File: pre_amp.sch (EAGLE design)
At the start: 51 parts, among them Q1 BF245, Q2 BF245, Q3 BF245

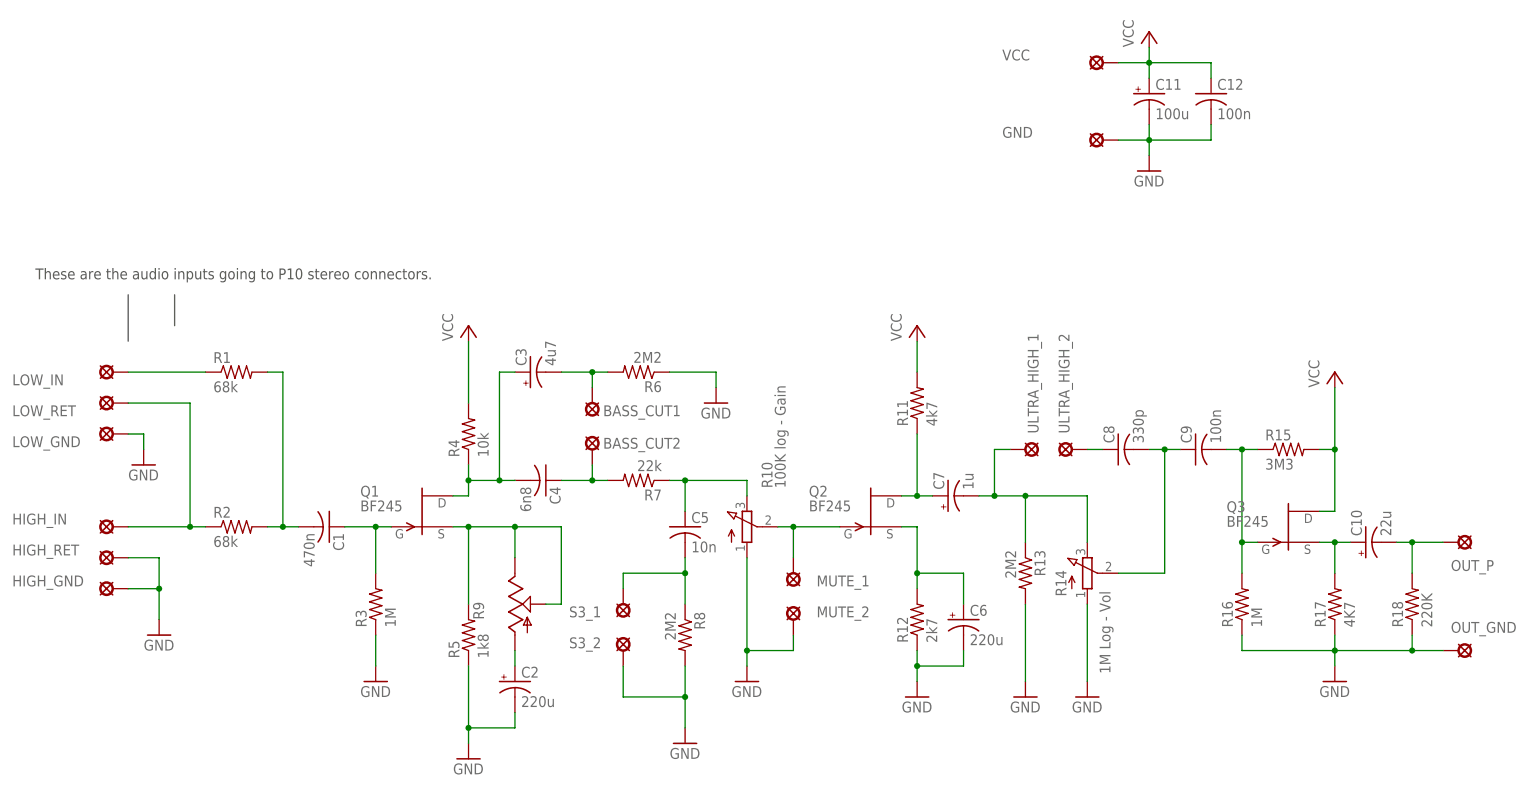
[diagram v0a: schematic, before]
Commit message: [#1] Improvements and fixes
Fixes ERC check errors:
R9 value set;
Approved FRAME have no value.

Better positioning some labels and texts.
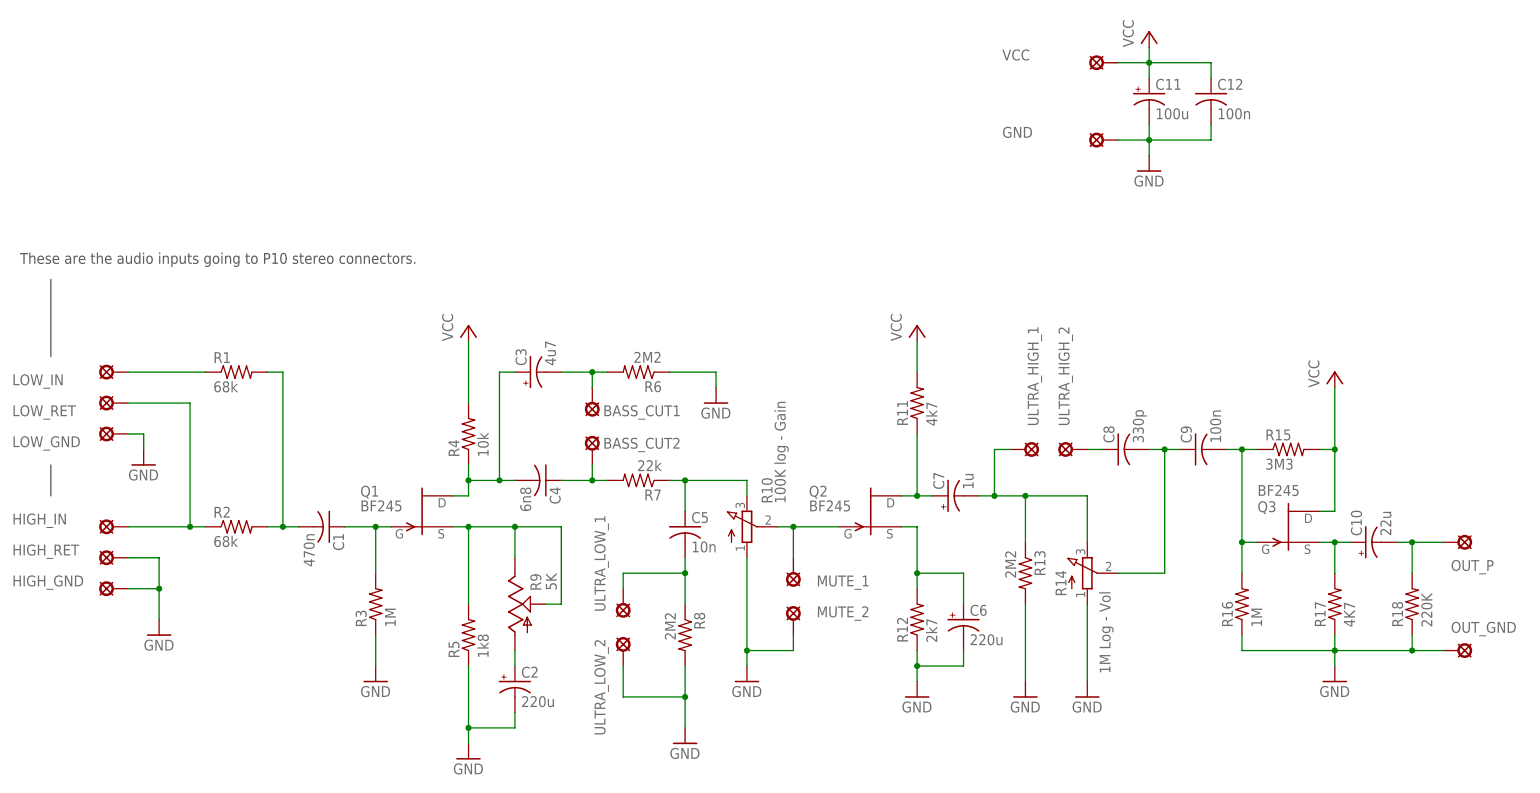
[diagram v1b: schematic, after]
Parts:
- R9: value (none) -> 5K
- renumbered S3_1 to ULTRA_LOW_1, S3_2 to ULTRA_LOW_2
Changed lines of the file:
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@@
 <part name="GND6" library="supply1" deviceset="GND" device=""/>
 <part name="P+1" library="supply1" deviceset="VCC" device=""/>
-<part name="R9" library="pot" deviceset="TRIM_US-" device="CA6V"/>
+<part name="R9" library="pot" deviceset="TRIM_US-" device="CA6V" value="5K"/>
 <part name="R10" library="pot" deviceset="3RP/1610N" device="" value="100K log - Gain"/>
 <part name="BASS_CUT1" library="solpad" deviceset="MCS08" device=""/>
 <part name="BASS_CUT2" library="solpad" deviceset="MCS08" device=""/>
-<part name="S3_1" library="solpad" deviceset="MCS08" device=""/>
-<part name="S3_2" library="solpad" deviceset="MCS08" device=""/>
+<part name="ULTRA_LOW_1" library="solpad" deviceset="MCS08" device=""/>
+<part name="ULTRA_LOW_2" library="solpad" deviceset="MCS08" device=""/>
 <part name="MUTE_1" library="solpad" deviceset="MCS08" device=""/>
 <part name="MUTE_2" library="solpad" deviceset="MCS08" device=""/>
@@
 <sheet>
 <plain>
-<text x="10.16" y="111.76" size="1.778" layer="97">These are the audio inputs going to P10 stereo connectors.</text>
-<wire x1="33.02" y1="109.22" x2="33.02" y2="104.14" width="0.1524" layer="97"/>
-<wire x1="25.4" y1="101.6" x2="25.4" y2="109.22" width="0.1524" layer="97"/>
+<text x="7.62" y="114.3" size="1.778" layer="97">These are the audio inputs going to P10 stereo connectors.</text>
+<wire x1="12.7" y1="81.28" x2="12.7" y2="76.2" width="0.1524" layer="97"/>
+<wire x1="12.7" y1="99.06" x2="12.7" y2="111.76" width="0.1524" layer="97"/>
 </plain>
 <instances>
@@
 <instance part="Q1" gate="G$1" x="73.66" y="73.66"/>
 <instance part="Q2" gate="G$1" x="147.32" y="73.66"/>
-<instance part="Q3" gate="G$1" x="215.9" y="71.12"/>
+<instance part="Q3" gate="G$1" x="215.9" y="71.12" smashed="yes">
+<attribute name="NAME" x="210.82" y="73.533" size="1.778" layer="95"/>
+<attribute name="VALUE" x="210.82" y="76.2" size="1.778" layer="96"/>
+</instance>
 <instance part="C4" gate="G$1" x="93.98" y="78.74" rot="R270"/>
 <instance part="C5" gate="G$1" x="116.84" y="71.12"/>
@@
 <instance part="GND6" gate="1" x="121.92" y="91.44"/>
 <instance part="P+1" gate="VCC" x="81.28" y="104.14"/>
-<instance part="R9" gate="G$1" x="88.9" y="58.42"/>
+<instance part="R9" gate="G$1" x="88.9" y="58.42" smashed="yes">
+<attribute name="NAME" x="91.44" y="63.5" size="1.778" layer="95" rot="R270"/>
+<attribute name="VALUE" x="93.98" y="63.5" size="1.778" layer="96" rot="R270"/>
+</instance>
 <instance part="R10" gate="G$1" x="127" y="71.12" smashed="yes">
-<attribute name="NAME" x="131.191" y="77.47" size="1.778" layer="95" rot="R90"/>
-<attribute name="VALUE" x="133.35" y="77.47" size="1.778" layer="96" rot="R90"/>
+<attribute name="NAME" x="131.191" y="74.93" size="1.778" layer="95" rot="R90"/>
+<attribute name="VALUE" x="133.35" y="74.93" size="1.778" layer="96" rot="R90"/>
 </instance>
 <instance part="BASS_CUT1" gate="G$1" x="101.6" y="91.44" smashed="yes" rot="R180">
@@
 <attribute name="NAME" x="103.378" y="83.947" size="1.778" layer="95"/>
 </instance>
-<instance part="S3_1" gate="G$1" x="106.68" y="58.42" smashed="yes" rot="R180">
-<attribute name="NAME" x="97.79" y="56.261" size="1.778" layer="95"/>
-</instance>
-<instance part="S3_2" gate="G$1" x="106.68" y="50.8" smashed="yes">
-<attribute name="NAME" x="97.79" y="51.181" size="1.778" layer="95"/>
+<instance part="ULTRA_LOW_1" gate="G$1" x="106.68" y="58.42" smashed="yes" rot="R180">
+<attribute name="NAME" x="103.759" y="57.15" size="1.778" layer="95" rot="R90"/>
+</instance>
+<instance part="ULTRA_LOW_2" gate="G$1" x="106.68" y="50.8" smashed="yes">
+<attribute name="NAME" x="103.759" y="36.83" size="1.778" layer="95" rot="R90"/>
 </instance>
 <instance part="MUTE_1" gate="G$1" x="134.62" y="63.5" smashed="yes" rot="R180">
@@
 <instance part="GND10" gate="1" x="182.88" y="43.18"/>
 <instance part="ULTRA_HIGH_2" gate="G$1" x="180.34" y="83.82" smashed="yes" rot="R90">
-<attribute name="NAME" x="178.181" y="102.87" size="1.778" layer="95" rot="R270"/>
+<attribute name="NAME" x="179.959" y="87.63" size="1.778" layer="95" rot="R90"/>
 </instance>
 <instance part="ULTRA_HIGH_1" gate="G$1" x="172.72" y="83.82" smashed="yes" rot="R270">
-<attribute name="NAME" x="173.101" y="102.87" size="1.778" layer="95" rot="R270"/>
+<attribute name="NAME" x="174.879" y="87.63" size="1.778" layer="95" rot="R90"/>
 </instance>
 <instance part="C9" gate="G$1" x="200.66" y="83.82" rot="R90"/>
@@
 <pinref part="GND5" gate="1" pin="GND"/>
 <wire x1="116.84" y1="48.26" x2="116.84" y2="43.18" width="0.1524" layer="91"/>
-<pinref part="S3_2" gate="G$1" pin="MP"/>
+<pinref part="ULTRA_LOW_2" gate="G$1" pin="MP"/>
 <wire x1="116.84" y1="43.18" x2="116.84" y2="38.1" width="0.1524" layer="91"/>
 <wire x1="106.68" y1="48.26" x2="106.68" y2="43.18" width="0.1524" layer="91"/>
@@
 <pinref part="R8" gate="G$1" pin="1"/>
 <wire x1="116.84" y1="66.04" x2="116.84" y2="63.5" width="0.1524" layer="91"/>
-<pinref part="S3_1" gate="G$1" pin="MP"/>
+<pinref part="ULTRA_LOW_1" gate="G$1" pin="MP"/>
 <wire x1="116.84" y1="63.5" x2="116.84" y2="58.42" width="0.1524" layer="91"/>
 <wire x1="106.68" y1="60.96" x2="106.68" y2="63.5" width="0.1524" layer="91"/>
@@
 </sheet>
 </sheets>
+<errors>
+</errors>
 </schematic>
 </drawing>

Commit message: [#1] Update component package
Update component package.
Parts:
- C4: device rcl:C-US375-203X418 -> rcl:C-US050-030X075
- C8: device rcl:C-US375-203X418 -> rcl:C-US050-025X075
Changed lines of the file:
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@@
 <grid distance="0.1" unitdist="inch" unit="inch" style="dots" multiple="1" display="yes" altdistance="0.01" altunitdist="inch" altunit="inch"/>
 <layers>
-<layer number="1" name="Top" color="4" fill="1" visible="no" active="no"/>
-<layer number="16" name="Bottom" color="1" fill="1" visible="no" active="no"/>
-<layer number="17" name="Pads" color="2" fill="1" visible="no" active="no"/>
-<layer number="18" name="Vias" color="2" fill="1" visible="no" active="no"/>
-<layer number="19" name="Unrouted" color="6" fill="1" visible="no" active="no"/>
-<layer number="20" name="Dimension" color="15" fill="1" visible="no" active="no"/>
-<layer number="21" name="tPlace" color="7" fill="1" visible="no" active="no"/>
-<layer number="22" name="bPlace" color="7" fill="1" visible="no" active="no"/>
-<layer number="23" name="tOrigins" color="15" fill="1" visible="no" active="no"/>
-<layer number="24" name="bOrigins" color="15" fill="1" visible="no" active="no"/>
-<layer number="25" name="tNames" color="7" fill="1" visible="no" active="no"/>
-<layer number="26" name="bNames" color="7" fill="1" visible="no" active="no"/>
-<layer number="27" name="tValues" color="7" fill="1" visible="no" active="no"/>
-<layer number="28" name="bValues" color="7" fill="1" visible="no" active="no"/>
+<layer number="1" name="Top" color="4" fill="1" visible="yes" active="no"/>
+<layer number="16" name="Bottom" color="1" fill="1" visible="yes" active="no"/>
+<layer number="17" name="Pads" color="2" fill="1" visible="yes" active="no"/>
+<layer number="18" name="Vias" color="2" fill="1" visible="yes" active="no"/>
+<layer number="19" name="Unrouted" color="6" fill="1" visible="yes" active="no"/>
+<layer number="20" name="Dimension" color="15" fill="1" visible="yes" active="no"/>
+<layer number="21" name="tPlace" color="7" fill="1" visible="yes" active="no"/>
+<layer number="22" name="bPlace" color="7" fill="1" visible="yes" active="no"/>
+<layer number="23" name="tOrigins" color="15" fill="1" visible="yes" active="no"/>
+<layer number="24" name="bOrigins" color="15" fill="1" visible="yes" active="no"/>
+<layer number="25" name="tNames" color="7" fill="1" visible="yes" active="no"/>
+<layer number="26" name="bNames" color="7" fill="1" visible="yes" active="no"/>
+<layer number="27" name="tValues" color="7" fill="1" visible="yes" active="no"/>
+<layer number="28" name="bValues" color="7" fill="1" visible="yes" active="no"/>
 <layer number="29" name="tStop" color="7" fill="3" visible="no" active="no"/>
 <layer number="30" name="bStop" color="7" fill="6" visible="no" active="no"/>
@@
 <layer number="35" name="tGlue" color="7" fill="4" visible="no" active="no"/>
 <layer number="36" name="bGlue" color="7" fill="5" visible="no" active="no"/>
-<layer number="37" name="tTest" color="7" fill="1" visible="no" active="no"/>
-<layer number="38" name="bTest" color="7" fill="1" visible="no" active="no"/>
+<layer number="37" name="tTest" color="7" fill="1" visible="yes" active="no"/>
+<layer number="38" name="bTest" color="7" fill="1" visible="yes" active="no"/>
 <layer number="39" name="tKeepout" color="4" fill="11" visible="no" active="no"/>
 <layer number="40" name="bKeepout" color="1" fill="11" visible="no" active="no"/>
@@
 <layer number="44" name="Drills" color="7" fill="1" visible="no" active="no"/>
 <layer number="45" name="Holes" color="7" fill="1" visible="no" active="no"/>
-<layer number="46" name="Milling" color="3" fill="1" visible="no" active="no"/>
-<layer number="47" name="Measures" color="7" fill="1" visible="no" active="no"/>
-<layer number="48" name="Document" color="7" fill="1" visible="no" active="no"/>
-<layer number="49" name="Reference" color="7" fill="1" visible="no" active="no"/>
-<layer number="51" name="tDocu" color="7" fill="1" visible="no" active="no"/>
-<layer number="52" name="bDocu" color="7" fill="1" visible="no" active="no"/>
+<layer number="46" name="Milling" color="3" fill="1" visible="yes" active="no"/>
+<layer number="47" name="Measures" color="7" fill="1" visible="yes" active="no"/>
+<layer number="48" name="Document" color="7" fill="1" visible="yes" active="no"/>
+<layer number="49" name="Reference" color="7" fill="1" visible="yes" active="no"/>
+<layer number="51" name="tDocu" color="7" fill="1" visible="yes" active="no"/>
+<layer number="52" name="bDocu" color="7" fill="1" visible="yes" active="no"/>
 <layer number="90" name="Modules" color="5" fill="1" visible="yes" active="yes"/>
 <layer number="91" name="Nets" color="2" fill="1" visible="yes" active="yes"/>
@@
 <part name="Q2" library="transistor-fet" deviceset="BF245" device=""/>
 <part name="Q3" library="transistor-fet" deviceset="BF245" device=""/>
-<part name="C4" library="rcl" deviceset="C-US" device="375-203X418" value="6n8"/>
+<part name="C4" library="rcl" deviceset="C-US" device="050-030X075" value="6n8"/>
 <part name="C5" library="rcl" deviceset="C-US" device="050-030X075" value="10n"/>
 <part name="LOW_IN" library="solpad" deviceset="MCS08" device=""/>
@@
 <part name="GND9" library="supply1" deviceset="GND" device=""/>
 <part name="R14" library="pot" deviceset="3RP/1610N" device="" value="1M Log - Vol"/>
-<part name="C8" library="rcl" deviceset="C-US" device="375-203X418" value="330p"/>
+<part name="C8" library="rcl" deviceset="C-US" device="050-025X075" value="330p"/>
 <part name="GND10" library="supply1" deviceset="GND" device=""/>
 <part name="ULTRA_HIGH_2" library="solpad" deviceset="MCS08" device=""/>

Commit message: [#1] PCB layout
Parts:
- C2: device resistor:CPOL-USE3.5-8 -> resistor:CPOL-USE5-8.5
- R5: device resistor:R-US_0204/7 -> resistor:R-US_0207/10
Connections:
- net GND: now also R5.2; no longer R5.1
- net N$4: now also R5.1; no longer R5.2
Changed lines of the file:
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@@
 </variantdefs>
 <classes>
-<class number="0" name="default" width="0" drill="0">
+<class number="0" name="default" width="1.016" drill="0">
+<clearance class="0" value="0.8128"/>
+</class>
+<class number="1" name="Power" width="1.2192" drill="0">
+<clearance class="1" value="1.016"/>
 </class>
 </classes>
@@
 <part name="R3" library="resistor" deviceset="R-US_" device="0204/7" value="1M"/>
 <part name="R4" library="resistor" deviceset="R-US_" device="0204/7" value="10k"/>
-<part name="R5" library="resistor" deviceset="R-US_" device="0204/7" value="1k8"/>
+<part name="R5" library="resistor" deviceset="R-US_" device="0207/10" value="1k8"/>
 <part name="R6" library="resistor" deviceset="R-US_" device="0204/7" value="2M2"/>
 <part name="R7" library="resistor" deviceset="R-US_" device="0204/7" value="22k"/>
 <part name="R8" library="resistor" deviceset="R-US_" device="0204/7" value="2M2"/>
 <part name="C1" library="resistor" deviceset="C-US" device="050-035X075" value="470n"/>
-<part name="C2" library="resistor" deviceset="CPOL-US" device="E3.5-8" value="220u"/>
+<part name="C2" library="resistor" deviceset="CPOL-US" device="E5-8.5" value="220u"/>
 <part name="C3" library="resistor" deviceset="CPOL-US" device="E2.5-6" value="4u7"/>
 <part name="Q1" library="transistor-fet" deviceset="BF245" device=""/>
@@
 <segment>
 <pinref part="Q1" gate="G$1" pin="S"/>
-<pinref part="R5" gate="G$1" pin="2"/>
+<pinref part="R5" gate="G$1" pin="1"/>
 <wire x1="78.74" y1="71.12" x2="81.28" y2="71.12" width="0.1524" layer="91"/>
-<wire x1="81.28" y1="71.12" x2="81.28" y2="58.42" width="0.1524" layer="91"/>
+<wire x1="81.28" y1="71.12" x2="81.28" y2="48.26" width="0.1524" layer="91"/>
 <pinref part="R9" gate="G$1" pin="E"/>
 <wire x1="88.9" y1="66.04" x2="88.9" y2="71.12" width="0.1524" layer="91"/>
@@
 </segment>
 </net>
-<net name="GND" class="0">
+<net name="GND" class="1">
 <segment>
 <pinref part="HIGH_RET" gate="G$1" pin="MP"/>
@@
 </segment>
 <segment>
-<pinref part="R5" gate="G$1" pin="1"/>
-<wire x1="81.28" y1="48.26" x2="81.28" y2="38.1" width="0.1524" layer="91"/>
+<pinref part="R5" gate="G$1" pin="2"/>
+<wire x1="81.28" y1="58.42" x2="81.28" y2="38.1" width="0.1524" layer="91"/>
 <pinref part="C2" gate="G$1" pin="-"/>
 <wire x1="81.28" y1="38.1" x2="88.9" y2="38.1" width="0.1524" layer="91"/>
@@
 </segment>
 </net>
-<net name="VCC" class="0">
+<net name="VCC" class="1">
 <segment>
 <pinref part="R4" gate="G$1" pin="2"/>
